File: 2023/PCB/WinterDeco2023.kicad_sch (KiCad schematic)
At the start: 42 parts, among them J1 CONN_ICSP_UART, Q1 IRLML6402, SW1 TOUCH_SENSOR, U1 PIC18F14 (SOP20/SSOP20)

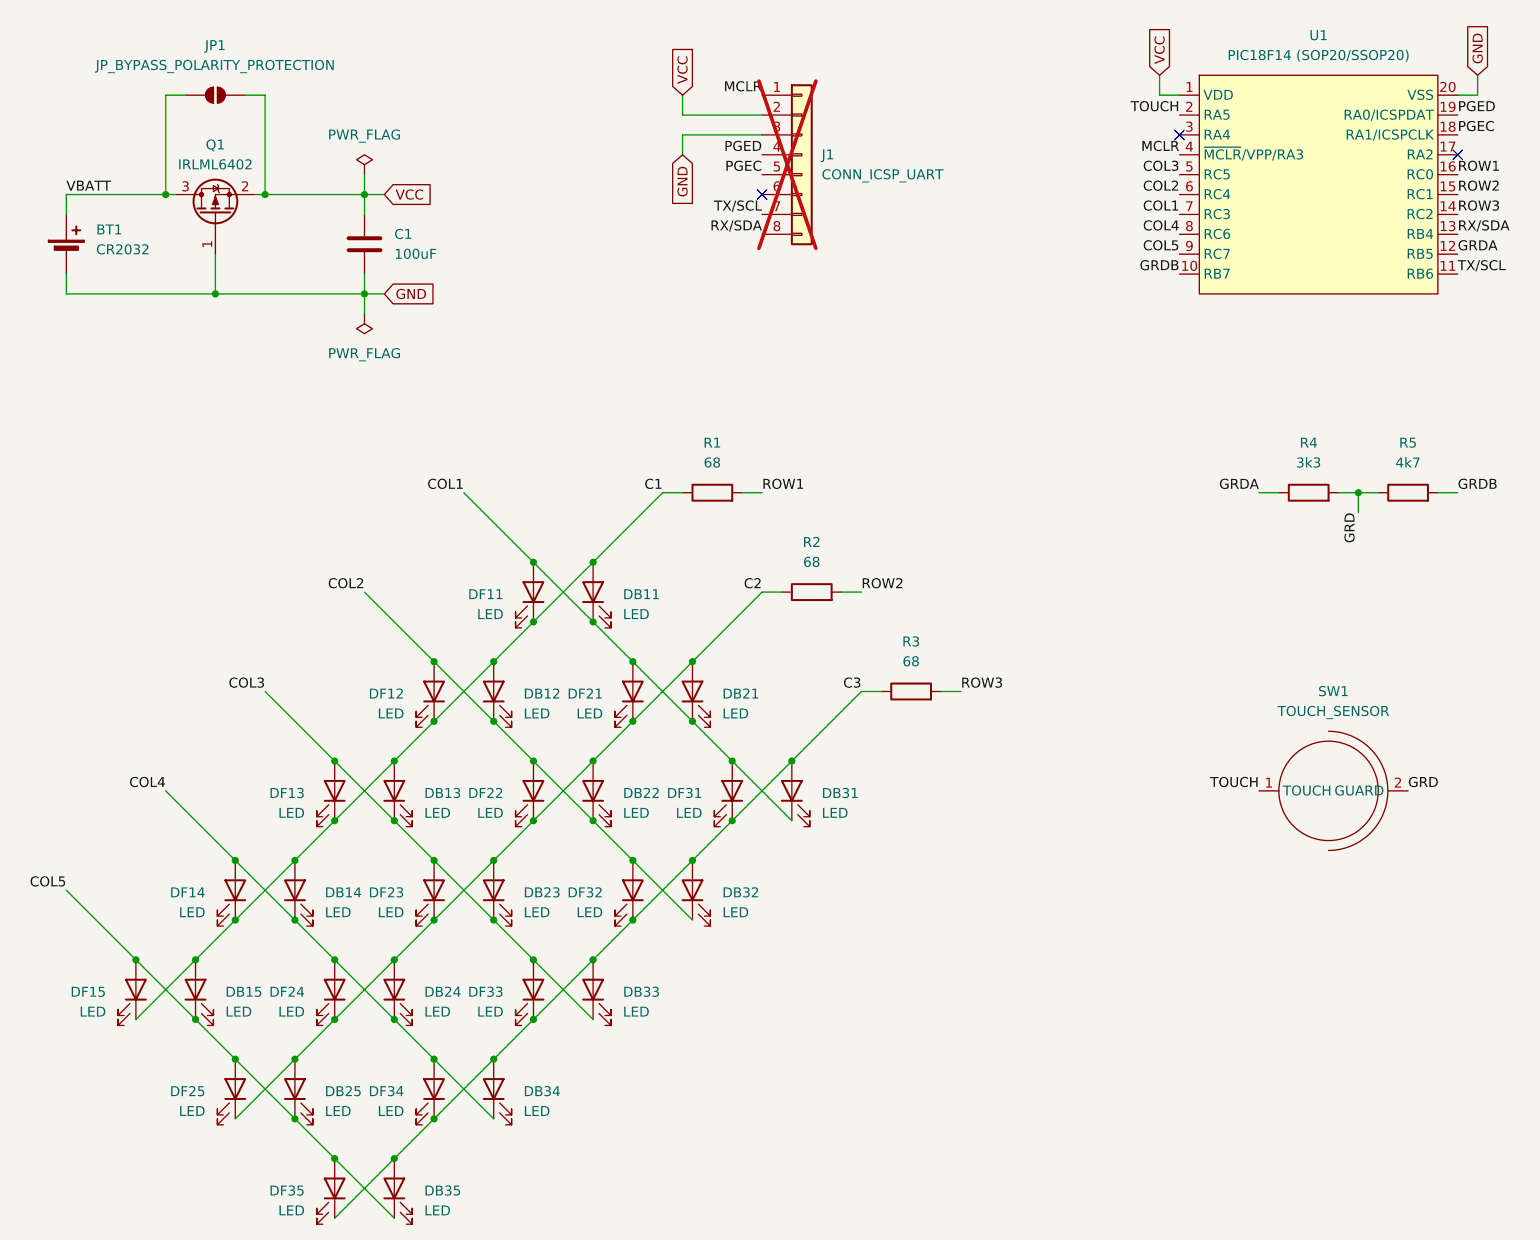
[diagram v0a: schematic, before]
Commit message: Fixed swapped rows and columns
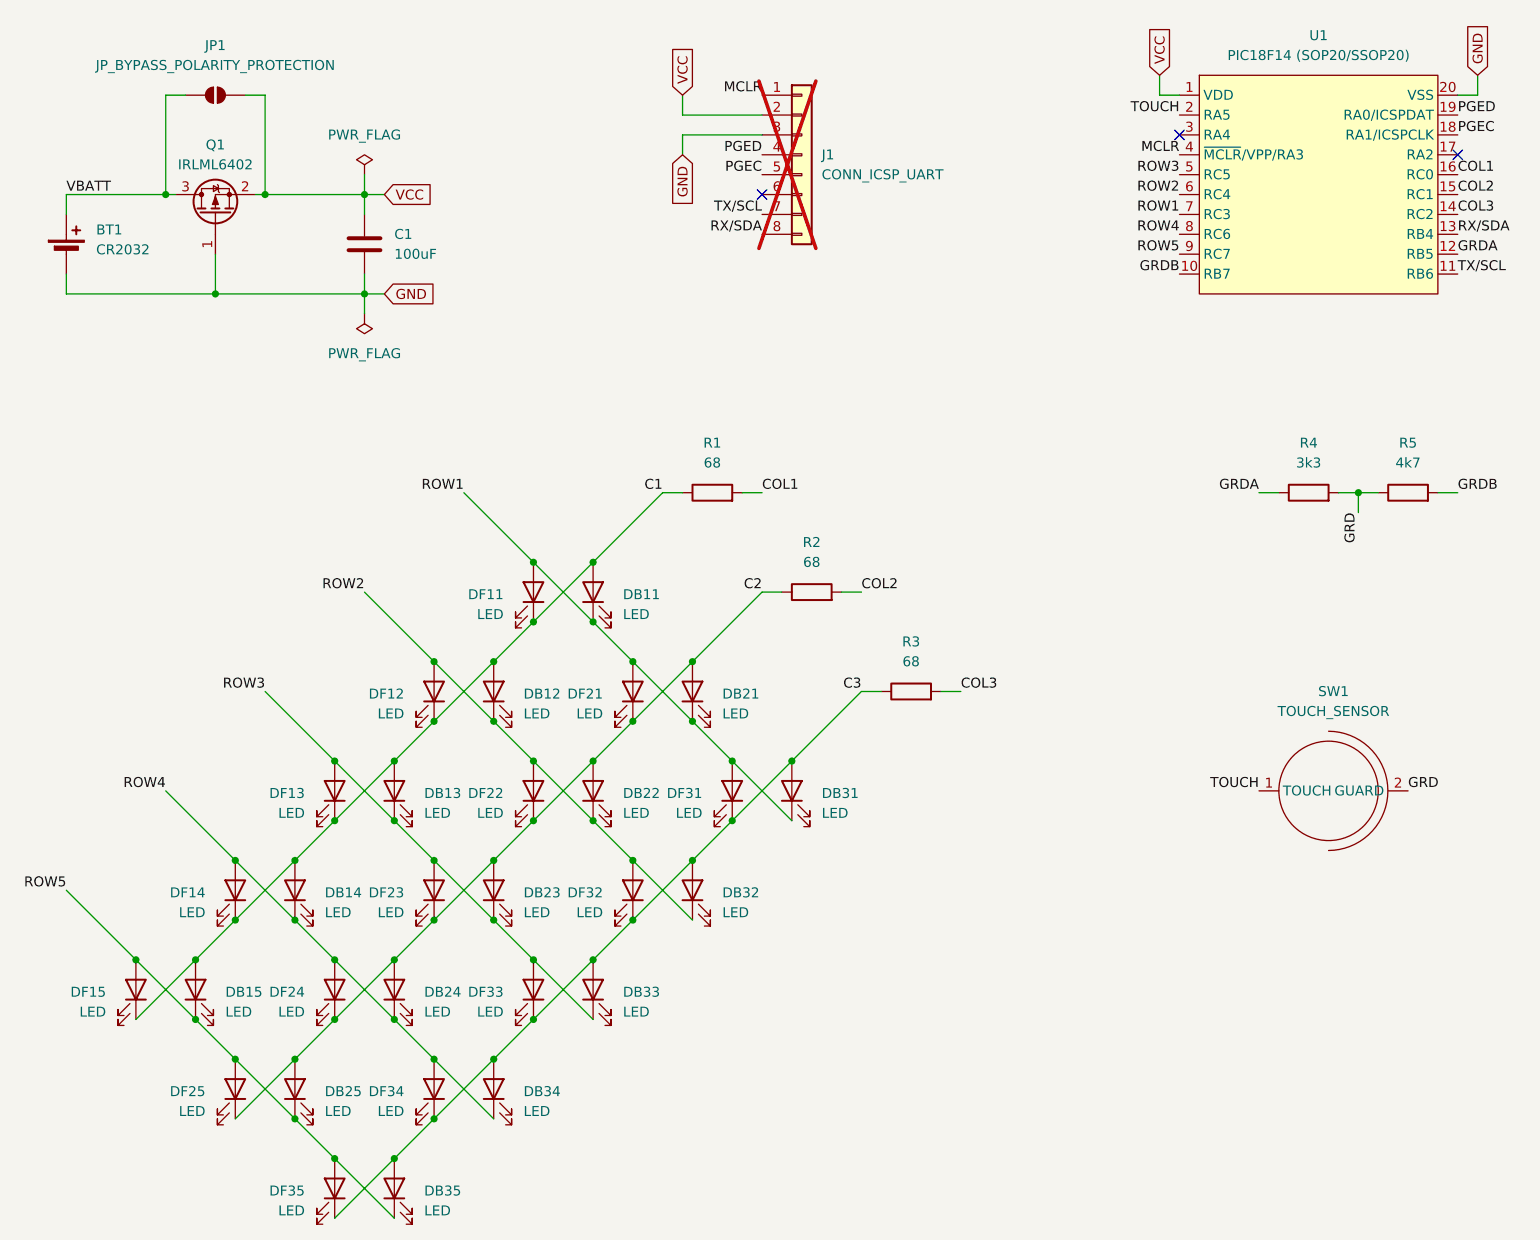
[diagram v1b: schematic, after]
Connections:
- net COL1: now also R1.2, U1.16 (RC0); no longer DB11.1 (K), DB21.1 (K), DB31.1 (K), DF11.2 (A), DF21.2 (A), DF31.2 (A), U1.7 (RC3)
- net COL2: now also R2.2, U1.15 (RC1); no longer DB12.1 (K), DB22.1 (K), DB32.1 (K), DF12.2 (A), DF22.2 (A), DF32.2 (A), U1.6 (RC4)
- net COL3: now also R3.2, U1.14 (RC2); no longer DB13.1 (K), DB23.1 (K), DB33.1 (K), DF13.2 (A), DF23.2 (A), DF33.2 (A), U1.5 (RC5)
- net ROW1: now also DB11.1 (K), DB21.1 (K), DB31.1 (K), DF11.2 (A), DF21.2 (A), DF31.2 (A), U1.7 (RC3); no longer R1.2, U1.16 (RC0)
- net ROW2: now also DB12.1 (K), DB22.1 (K), DB32.1 (K), DF12.2 (A), DF22.2 (A), DF32.2 (A), U1.6 (RC4); no longer R2.2, U1.15 (RC1)
- net ROW3: now also DB13.1 (K), DB23.1 (K), DB33.1 (K), DF13.2 (A), DF23.2 (A), DF33.2 (A), U1.5 (RC5); no longer R3.2, U1.14 (RC2)
- net COL4 renamed ROW4
- net COL5 renamed ROW5
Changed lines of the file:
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@@
 	)
 	(label "COL2"
-		(at 193.04 50.8 180)
-		(effects
-			(font
-				(size 1.27 1.27)
-			)
-			(justify right bottom)
+		(at 228.6 50.8 0)
+		(effects
+			(font
+				(size 1.27 1.27)
+			)
+			(justify left bottom)
 		)
 	)
@@
 	)
 	(label "ROW1"
-		(at 228.6 48.26 0)
-		(effects
-			(font
-				(size 1.27 1.27)
-			)
-			(justify left bottom)
+		(at 193.04 53.34 180)
+		(effects
+			(font
+				(size 1.27 1.27)
+			)
+			(justify right bottom)
 		)
 	)
@@
 	)
 	(label "COL3"
-		(at 193.04 48.26 180)
-		(effects
-			(font
-				(size 1.27 1.27)
-			)
-			(justify right bottom)
+		(at 228.6 53.34 0)
+		(effects
+			(font
+				(size 1.27 1.27)
+			)
+			(justify left bottom)
 		)
 	)
 	(label "COL2"
-		(at 88.9 101.6 180)
-		(effects
-			(font
-				(size 1.27 1.27)
-			)
-			(justify right bottom)
+		(at 152.4 101.6 0)
+		(effects
+			(font
+				(size 1.27 1.27)
+			)
+			(justify left bottom)
 		)
 	)
 	(label "COL1"
-		(at 101.6 88.9 180)
-		(effects
-			(font
-				(size 1.27 1.27)
-			)
-			(justify right bottom)
+		(at 139.7 88.9 0)
+		(effects
+			(font
+				(size 1.27 1.27)
+			)
+			(justify left bottom)
 		)
 	)
@@
 	)
 	(label "ROW3"
+		(at 76.2 114.3 180)
+		(effects
+			(font
+				(size 1.27 1.27)
+			)
+			(justify right bottom)
+		)
+	)
+	(label "COL3"
 		(at 165.1 114.3 0)
 		(effects
@@
 		)
 	)
-	(label "COL3"
-		(at 76.2 114.3 180)
-		(effects
-			(font
-				(size 1.27 1.27)
-			)
-			(justify right bottom)
-		)
-	)
 	(label "ROW2"
-		(at 228.6 50.8 0)
-		(effects
-			(font
-				(size 1.27 1.27)
-			)
-			(justify left bottom)
+		(at 193.04 50.8 180)
+		(effects
+			(font
+				(size 1.27 1.27)
+			)
+			(justify right bottom)
 		)
 	)
@@
 	)
 	(label "ROW3"
-		(at 228.6 53.34 0)
-		(effects
-			(font
-				(size 1.27 1.27)
-			)
-			(justify left bottom)
+		(at 193.04 48.26 180)
+		(effects
+			(font
+				(size 1.27 1.27)
+			)
+			(justify right bottom)
 		)
 	)
@@
 	)
 	(label "ROW1"
-		(at 139.7 88.9 0)
-		(effects
-			(font
-				(size 1.27 1.27)
-			)
-			(justify left bottom)
+		(at 101.6 88.9 180)
+		(effects
+			(font
+				(size 1.27 1.27)
+			)
+			(justify right bottom)
 		)
 	)
@@
 	)
 	(label "COL1"
-		(at 193.04 53.34 180)
-		(effects
-			(font
-				(size 1.27 1.27)
-			)
-			(justify right bottom)
-		)
-	)
-	(label "COL4"
+		(at 228.6 48.26 0)
+		(effects
+			(font
+				(size 1.27 1.27)
+			)
+			(justify left bottom)
+		)
+	)
+	(label "ROW4"
 		(at 193.04 55.88 180)
 		(effects
@@
 	)
 	(label "ROW2"
-		(at 152.4 101.6 0)
-		(effects
-			(font
-				(size 1.27 1.27)
-			)
-			(justify left bottom)
+		(at 88.9 101.6 180)
+		(effects
+			(font
+				(size 1.27 1.27)
+			)
+			(justify right bottom)
 		)
 	)
@@
 		)
 	)
-	(label "COL5"
+	(label "ROW5"
 		(at 50.8 139.7 180)
 		(effects
@@
 		)
 	)
-	(label "COL4"
+	(label "ROW4"
 		(at 63.5 127 180)
 		(effects
@@
 		)
 	)
-	(label "COL5"
+	(label "ROW5"
 		(at 193.04 58.42 180)
 		(effects
